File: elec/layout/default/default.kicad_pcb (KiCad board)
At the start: 4 copper layers, 76 x 155 mm, 111 parts, among them J1 ?, J2 ?, Q1 ?, SW1 ?, SW10 ?, SW11 ?, SW12 ?, SW13 ?, SW14 ?, SW15 ?, SW16 ?, SW17 ?, SW18 ?, SW19 ?, SW2 ?, SW20 ?, SW21 ?, SW22 ?, SW23 ?, SW24 ?, SW25 ?, SW26 ?, SW27 ?, SW28 ?, SW29 ?, SW3 ?, SW30 ?, SW31 ?, SW32 ?, SW33 ?, SW34 ?, SW35 ?, SW36 ?, SW37 ?, SW38 ?, SW39 ?, SW4 ?, SW40 ?, SW5 ?, SW6 ?, SW7 ?, SW8 ?, SW9 ?, U1 ?, U2 ?, U3 ?, U4 ?, U5 ?, U6 ?, U7 ?, U8 ?

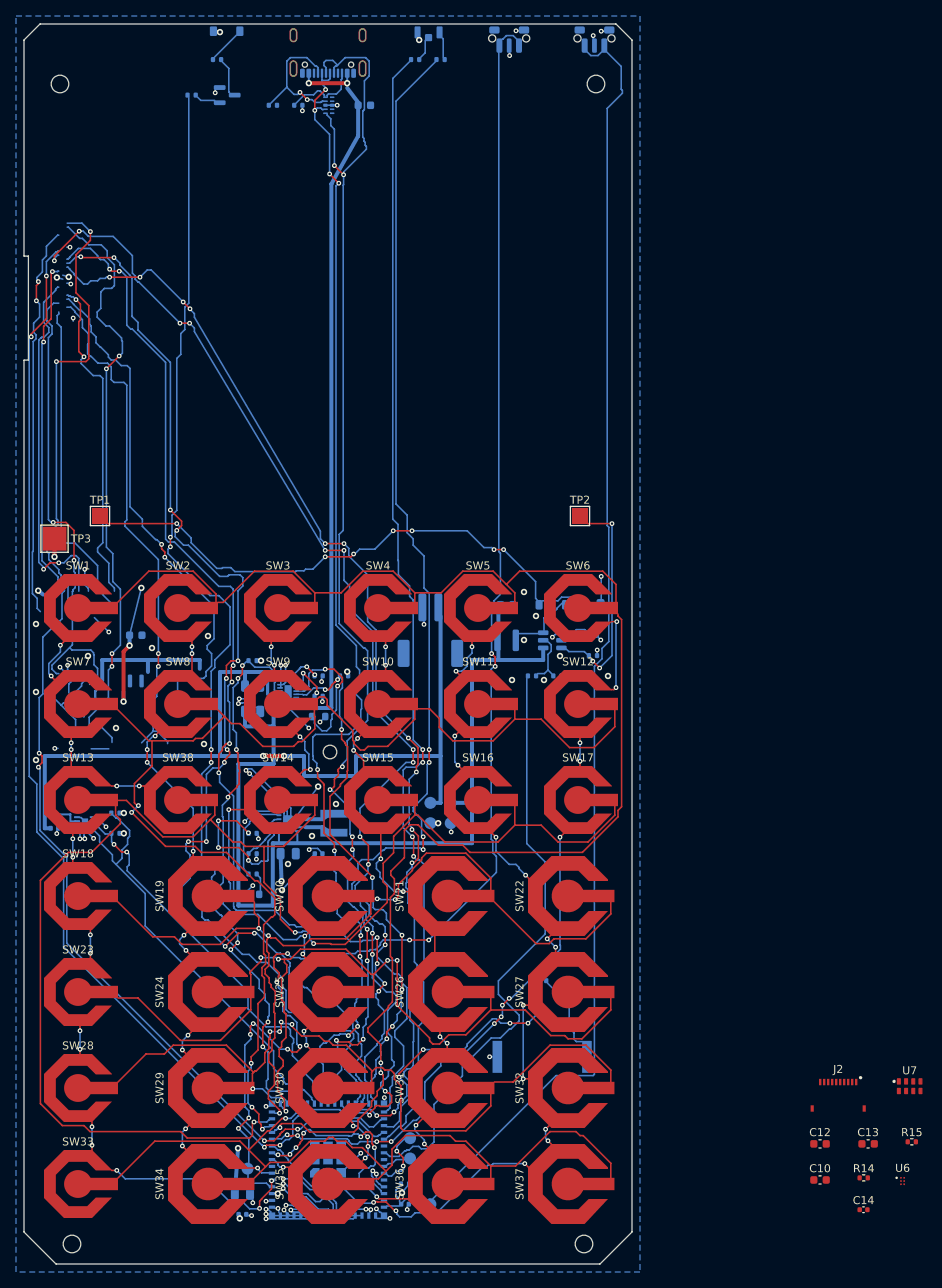
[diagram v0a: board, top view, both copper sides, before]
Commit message: mip: place and route the MIP board
- Placed all 111 parts (placement-ids re-recorded); J2 guard now checks for
  the FH34SRJ footprint; the grid check measures below-drop parts before
  the 11 mm drop.
- Stripped the stale e-paper-era signal copper: after the stretch and the
  net renames no tool recognised it, so route_signals had left it in place,
  dangling at the old connector's pads. Every signal is rerouted from
  scratch: 98 nets, 2052 segments, 291 vias, exact audit clean.
- route_power: sys now reaches the panel boost (U6, L2, C11), hopping bat's
  loop on F.Cu between the SW8 and SW9 dome keepouts.
- route_signals: nudge_vias moves a via the grid left a hair under the
  clearance rule, rather than failing the audit.
- U5's embedded antenna zone moved with the stretch; mounting holes, dome
  keepouts and stitching re-run; panel models re-attached to TP3.

check_pour, check_ends, check_placement, route_power --check and
check_netlist all pass.

Co-Authored-By: Claude Opus 5.5 (1M context) <noreply@anthropic.com>
Claude-Session: https://claude.ai/code/session_01Fsrot3PauY1JdFC7HgzJ33
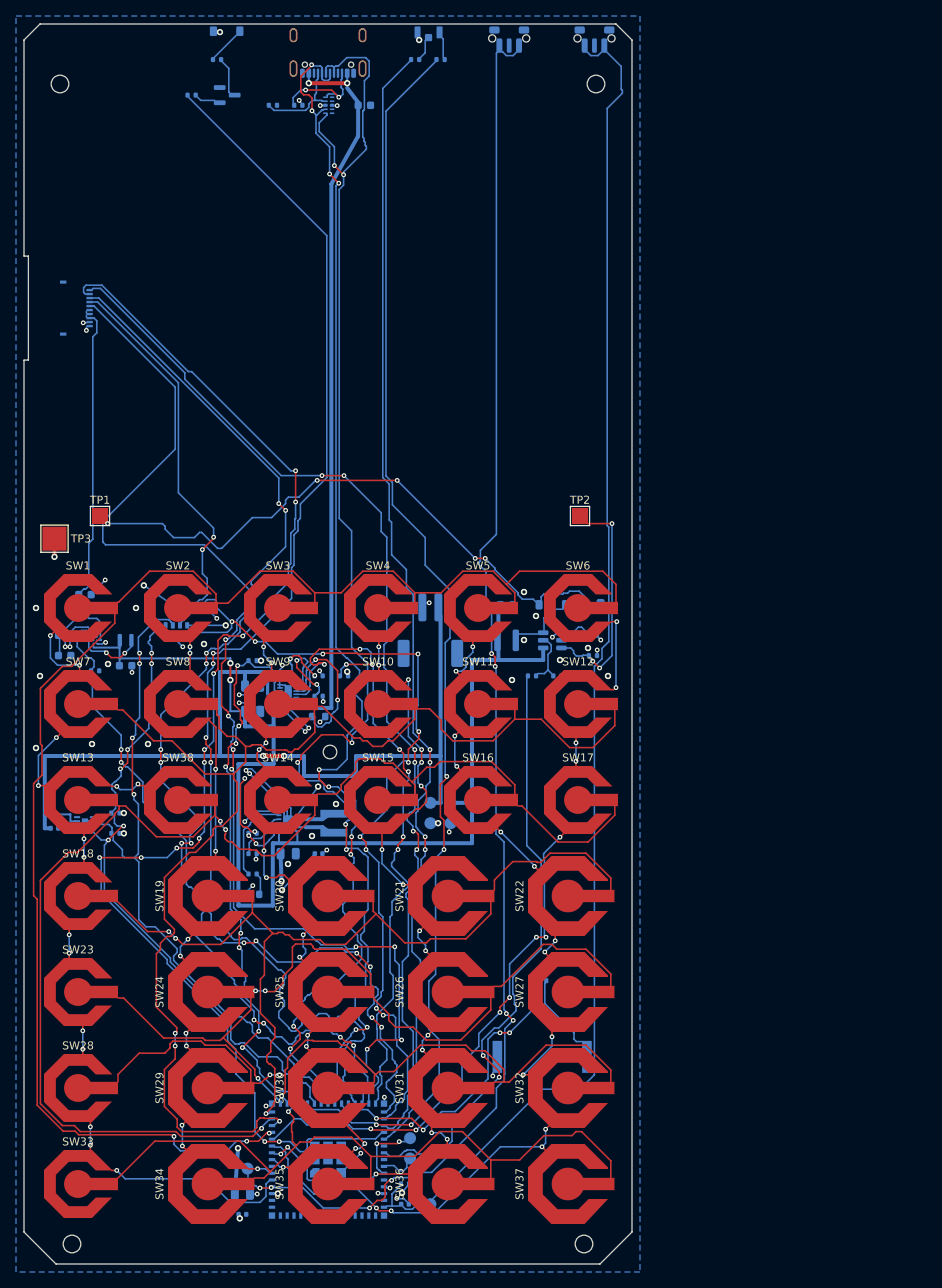
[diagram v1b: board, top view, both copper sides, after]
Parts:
- C10, C12, C13, C14, J2, R14, R15, U6, U7: moved to B.Cu
- moved J2 134.6 mm to (8.20, 35.5), turned to 90 degrees
- moved U6 121.5 mm to (8.89, 77.0)
- moved C13 117.5 mm to (5.08, 78.9)
- moved C10 117.5 mm to (7.62, 71.3)
- moved R14 115.1 mm to (8.89, 80.8)
- moved C14 114.4 mm to (19.1, 72.6)
- moved C12 113.8 mm to (5.08, 76.4)
- moved R15 110.8 mm to (22.9, 72.6)
- moved U7 107.9 mm to (19.1, 75.8)
- moved L2 5.24 mm to (12.7, 77.0)
- moved C11 4.02 mm to (12.7, 80.2)
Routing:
- net (no net): track 535.9 -> 0.00 mm, vias 18 -> 0
- net gnd: track 153.4 -> 81.8 mm, vias 84 -> 60
- net mip_pwr: track 145.9 -> 93.6 mm, vias 12 -> 8
- net extcomin: track 0.00 -> 49.1 mm, vias 0 -> 2
- net v5: track 0.00 -> 48.7 mm
- net mip_clkoe: track 144.2 -> 105.2 mm, vias 4 -> 10
- net i2c_scl: track 48.4 -> 84.6 mm, vias 2 -> 4
- net i2c_sda: track 54.1 -> 80.8 mm, vias 0 -> 6
- net row2: track 183.2 -> 158.1 mm
- net mip_mosi: track 141.2 -> 164.3 mm, vias 6 -> 12
- net col2: track 52.5 -> 31.9 mm, vias 14 -> 13
- net chg_stat: track 66.9 -> 85.2 mm
- net row4: track 111.2 -> 94.8 mm, vias 5 -> 3
- net ir_led: track 147.3 -> 162.6 mm
- net cfg1: track 20.4 -> 6.01 mm, vias 4 -> 2
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
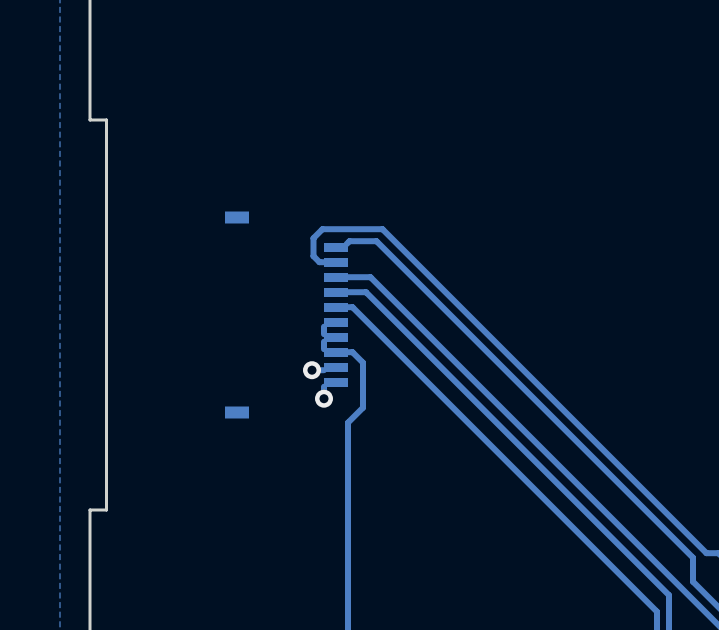
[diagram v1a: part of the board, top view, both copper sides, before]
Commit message: mip: glass flush left, J2 to X 7.05; shelved
The LS032 glass now sits at X 0..76, flush with the board (Barnaby, 1 Oct),
and J2 moves to X 7.05 so the tail keeps its 2 mm slack. Panel model and
docs updated. The signal reroute for the new J2 position did not pass its
audit (one gnd via 0.186 mm from usb_dm), so the board's mip_* tracks
still end at the old pads; docs/mip-display.md says how to resume.
Branch shelved for the Displaytech 64128M work.

Co-Authored-By: Claude Opus 5.5 (1M context) <noreply@anthropic.com>
Claude-Session: https://claude.ai/code/session_01Fsrot3PauY1JdFC7HgzJ33
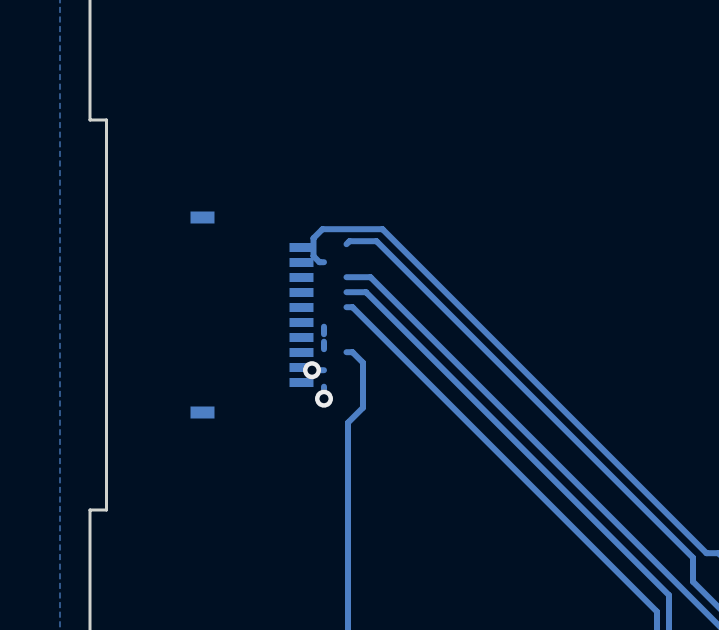
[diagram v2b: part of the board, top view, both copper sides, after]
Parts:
- moved J2 1.15 mm to (7.05, 35.5)
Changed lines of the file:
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@@
 	(footprint "hp42s:Hirose_FH34SRJ-10S-0.5SH_1x10-1MP_P0.50mm_Horizontal"
 		(layer "B.Cu")
-		(at 8.2 35.51 90)
+		(at 7.05 35.51 90)
 		(descr "Hirose FH34SRJ-10S-0.5SH(50), 10 way 0.5 mm FPC, top and bottom contact, back-flip actuator, 1.0 mm high. Lands from the FH34 catalogue recommended PCB mounting pattern. FPC enters from +y; contact 1 at +x. The LS032B7DD02 MIP panel's connector.")
 		(tags "FPC FFC connector Hirose FH34SRJ 0.5mm")

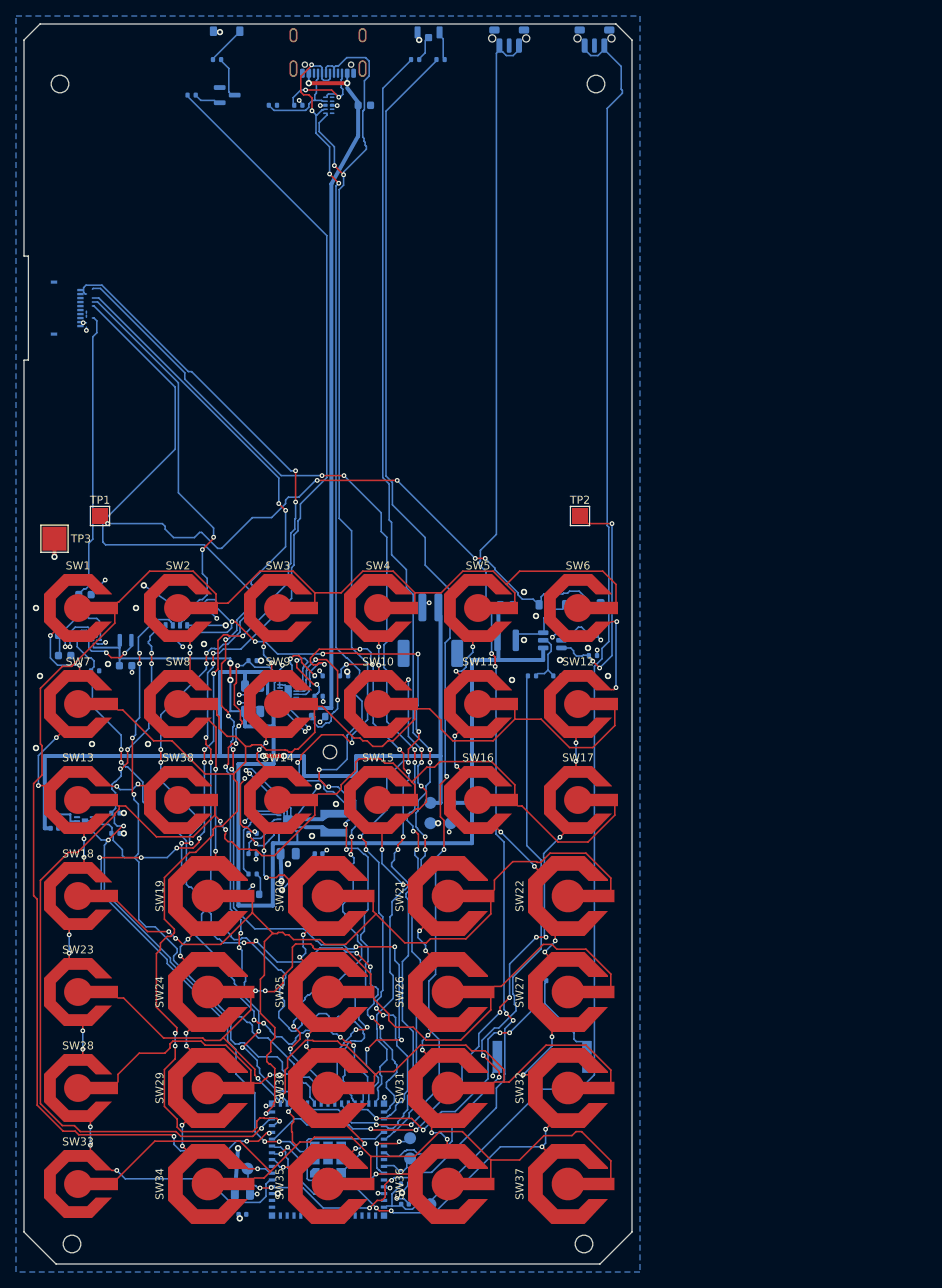
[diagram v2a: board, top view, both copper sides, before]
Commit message: mip: resumed; full reroute with the glass flush left and J2 at X 7.05
Strip and route from scratch after merging main: 96 nets, 0 failed, audit,
check_ends, check_pour and check_placement clean, every NPTH cleared by
0.25 mm. The gnd via that blocked the last reroute is gone.

Co-Authored-By: Claude Opus 5.5 (1M context) <noreply@anthropic.com>
Claude-Session: https://claude.ai/code/session_01Fsrot3PauY1JdFC7HgzJ33
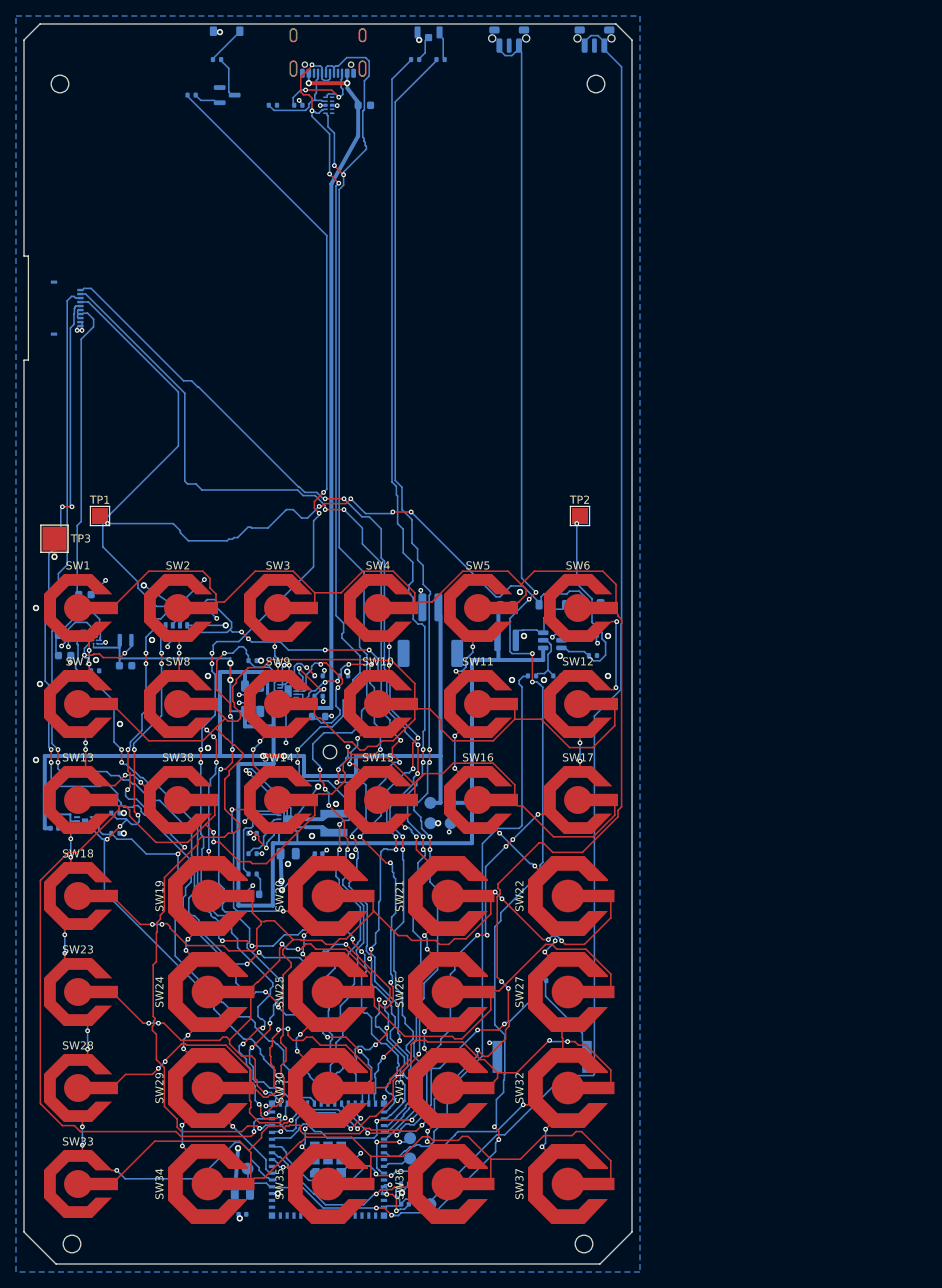
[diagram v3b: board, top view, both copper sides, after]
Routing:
- net mip_mosi: track 164.3 -> 138.8 mm, vias 12 -> 6
- net col3: track 62.7 -> 45.2 mm, vias 17 -> 13
- net mip_disp: track 147.7 -> 130.7 mm
- net row1: track 160.1 -> 176.6 mm, vias 3 -> 1
- net row5: track 86.9 -> 99.6 mm, vias 3 -> 7
- net col2: track 31.9 -> 43.7 mm
- net chg_stat2: track 70.9 -> 79.8 mm, vias 8 -> 6
- net boot: track 176.7 -> 185.3 mm
- net ir_led: track 162.6 -> 171.0 mm, vias 4 -> 12
- net usb_dp: track 168.2 -> 159.9 mm, vias 8 -> 6
- net col4: track 74.8 -> 67.2 mm, vias 14 -> 13
- net col0: track 58.8 -> 51.5 mm
- net i2c_scl: track 84.6 -> 91.3 mm, vias 4 -> 6
- net extcomin: track 49.1 -> 54.6 mm, vias 2 -> 0
- net led_red: track 156.4 -> 151.2 mm, vias 4 -> 6
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
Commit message: mip: 146 board, WROOM-1-N16R2, SPI NAND, no frontlight
- Source: frontlight and sliver removed; ESP32-S3-WROOM-1-N16R2 replaces
  the MINI-1-N8 (mip_cs IO40, mip_disp IO45); MT29F2G01 2 Gbit SPI NAND
  (W25N02KV drop-in) on the panel's SCK/MOSI, CS# IO41 + 10k, SO IO42.
- Footprints: hp42s:ESP32-S3-WROOM-1 (KiCad 10's, no thermal vias, antenna
  keepout allows the dome pads), hp42s:SPI_NAND_UPDFN-8_8x6mm_P1.27mm.
- Board: tools/mip_shorten_146.py -- glass Y 7.5..54.52, J2 and notch up
  4.5, everything below Y 59.3 up 9, board 76 x 146; holes A/B up to Y 3.5;
  faceplate pad into the keypad; frontlight parts and all copper removed.
- place_board.py tables in the post-import designators; route_power,
  check_placement, mech_models, jlc_bom updated.

Co-Authored-By: Claude Opus 5.5 (1M context) <noreply@anthropic.com>
Claude-Session: https://claude.ai/code/session_01Fsrot3PauY1JdFC7HgzJ33
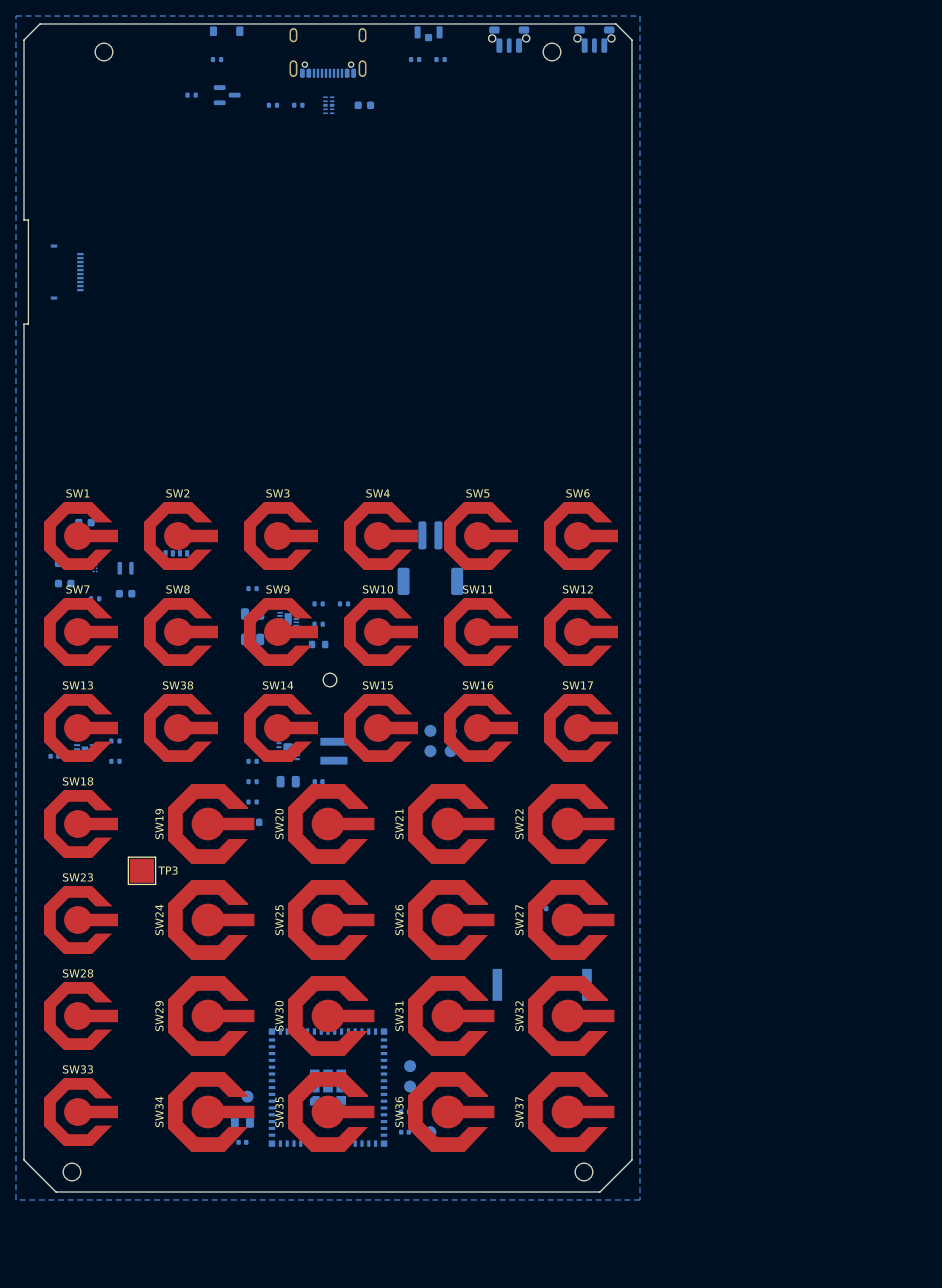
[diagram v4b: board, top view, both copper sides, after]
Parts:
- removed C15: ?, Capacitor_SMD:C_0805_2012Metric
- removed C16: ?, Capacitor_SMD:C_0603_1608Metric
- removed C17: ?, Capacitor_SMD:C_0402_1005Metric
- removed D3: ?, Diode_SMD:D_SOD-123
- removed L3: ?, Inductor_SMD:L_APV_ANR3015
- removed R21, R22, R23: ?, Resistor_SMD:R_0402_1005Metric
- removed TP1, TP2: ?, TestPoint:TestPoint_Pad_2.0x2.0mm
- removed U8: ?, Package_TO_SOT_SMD:SOT-23-6
- moved TP3 42.9 mm to (14.8, 105.9)
- moved LS1 9.00 mm to (64.8, 120.1)
- moved BT1 9.00 mm to (50.8, 66.8)
- moved C10 9.00 mm to (7.62, 62.3)
- moved C11 9.00 mm to (12.7, 71.2)
- moved C12 9.00 mm to (5.08, 67.4)
- moved C13 9.00 mm to (5.08, 69.9)
- moved C14 9.00 mm to (19.1, 63.6)
- moved C2 9.00 mm to (28.6, 73.8)
- moved C3 9.00 mm to (28.6, 76.9)
- moved C4 9.00 mm to (33.0, 94.7)
- moved C5 9.00 mm to (36.8, 94.7)
- moved C6 9.00 mm to (3.81, 91.5)
- moved C7 9.00 mm to (47.6, 138.5)
- moved C8 9.00 mm to (27.3, 137.3)
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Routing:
- net boot: track 185.3 -> 0.00 mm, vias 8 -> 0
- net row0: track 185.0 -> 0.00 mm, vias 5 -> 0
- net row1: track 176.6 -> 0.00 mm, vias 1 -> 0
- net ir_led: track 171.0 -> 0.00 mm, vias 12 -> 0
- net en: track 165.7 -> 0.00 mm
- net row2: track 161.1 -> 0.00 mm, vias 3 -> 0
- net usb_dp: track 159.9 -> 0.00 mm, vias 6 -> 0
- net usb_dm: track 153.1 -> 0.00 mm, vias 8 -> 0
- net led_red: track 151.2 -> 0.00 mm, vias 6 -> 0
- net sys: track 147.3 -> 0.00 mm, vias 2 -> 0
- net led_green: track 143.5 -> 0.00 mm, vias 4 -> 0
- net mip_cs: track 143.0 -> 0.00 mm, vias 8 -> 0
- net mip_mosi: track 138.8 -> 0.00 mm, vias 6 -> 0
- net mip_sck: track 135.5 -> 0.00 mm, vias 8 -> 0
- net mip_disp: track 130.7 -> 0.00 mm, vias 8 -> 0
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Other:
- board size 76 x 155 mm -> 76 x 146 mm
